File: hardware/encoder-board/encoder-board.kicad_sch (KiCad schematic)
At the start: 26 parts, among them J1 Conn_01x04, U1 ITR1204SR10A_TR(BY), U2 ITR1204SR10A_TR(BY), U3 LM2903

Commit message: various experiments with firmware. Nothing is working yet
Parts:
- R5: value 30 -> 130
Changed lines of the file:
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@@
 		(fields_autoplaced yes)
 		(property "Reference" "R5"
-			(at 207.01 54.61 0)
+			(at 207.01 54.6099 0)
 			(effects
 				(font
@@
 			)
 		)
-		(property "Value" "30"
-			(at 207.01 57.15 0)
+		(property "Value" "130"
+			(at 207.01 57.1499 0)
 			(effects
 				(font

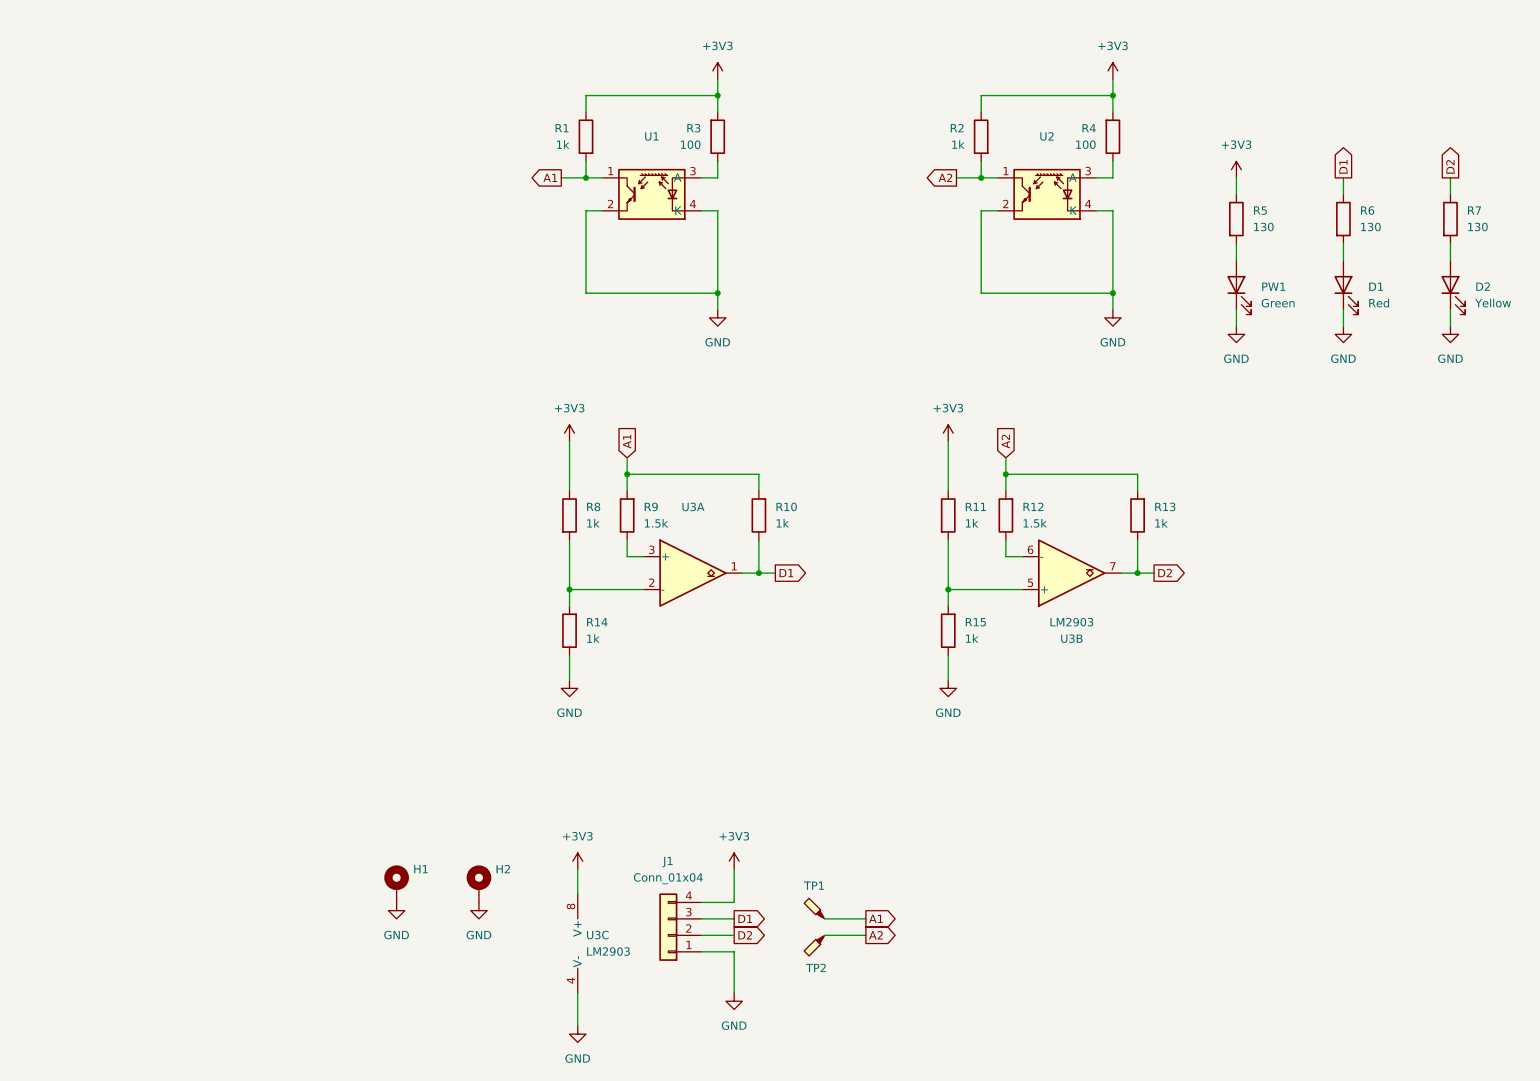
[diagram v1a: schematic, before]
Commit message: simplify encoder board to output analog output
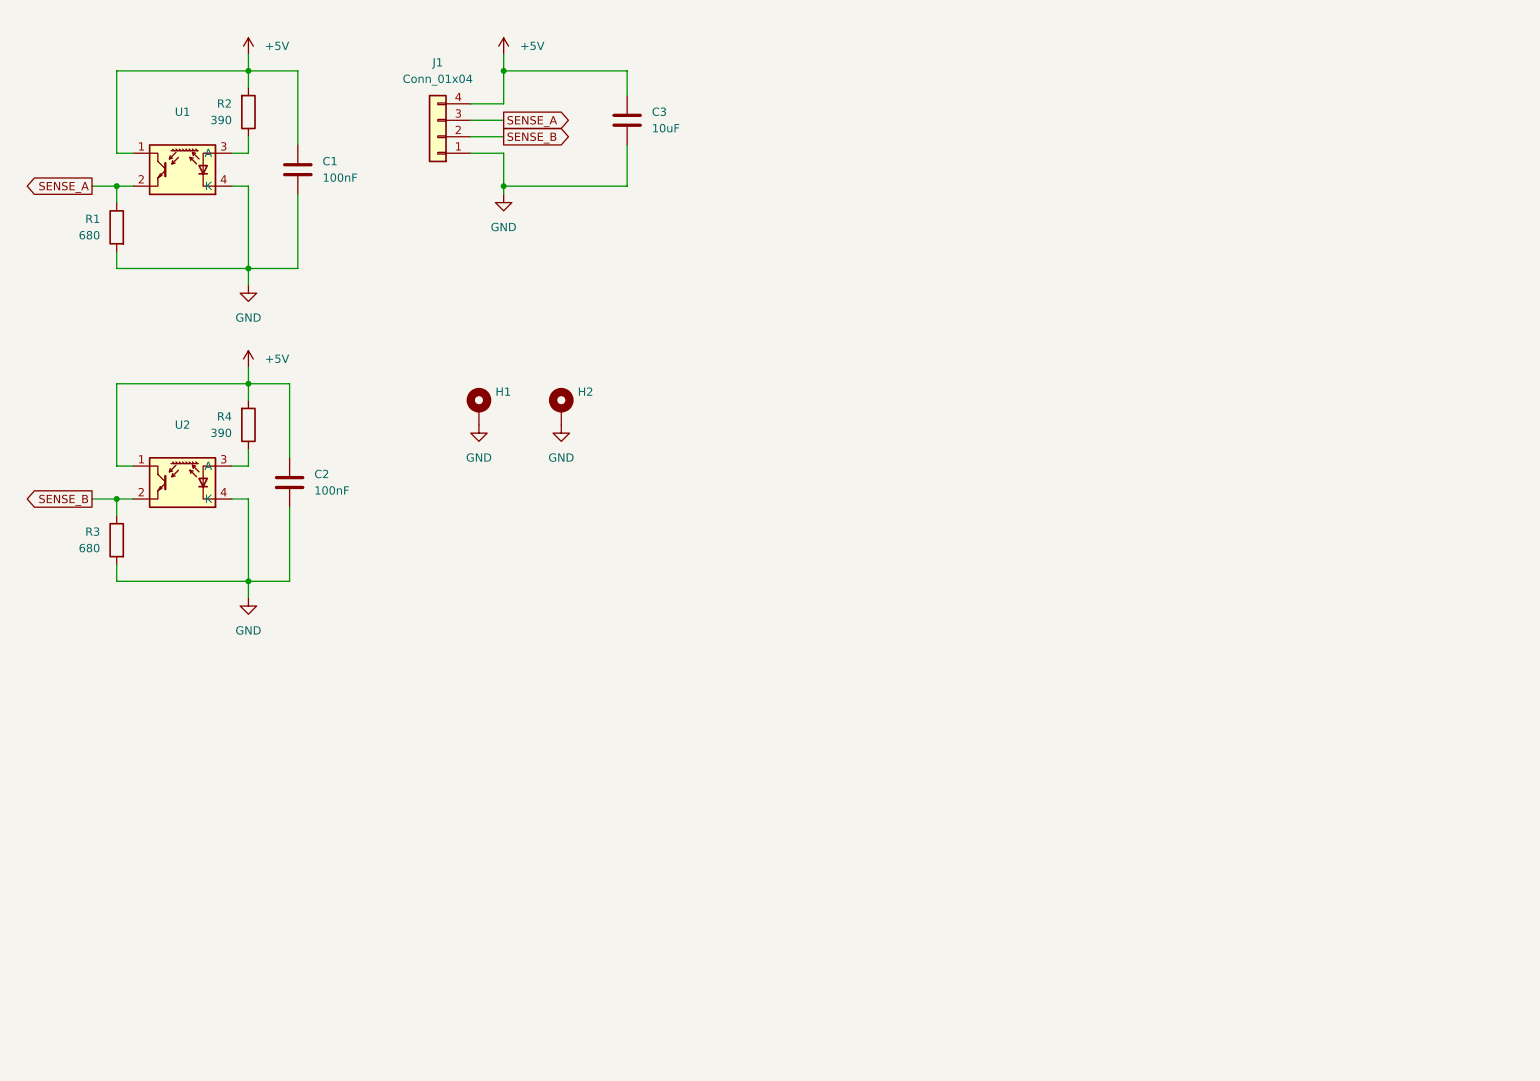
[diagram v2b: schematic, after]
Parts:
- removed D1: Red, LED_SMD:LED_0603_1608Metric, symbol Device:LED
- removed D2: Yellow, LED_SMD:LED_0603_1608Metric, symbol Device:LED
- removed PW1: Green, LED_SMD:LED_0603_1608Metric, symbol Device:LED
- removed R10, R11, R13, R14, R15, R8: 1k, Resistor_SMD:R_0603_1608Metric, symbol Device:R
- removed R12, R9: 1.5k, Resistor_SMD:R_0603_1608Metric, symbol Device:R
- removed R5, R6, R7: 130, Resistor_SMD:R_0603_1608Metric, symbol Device:R
- removed TP1, TP2: ~, TestPoint:TestPoint_Pad_D1.0mm, symbol Connector:TestPoint_Probe
- removed U3: LM2903, Package_SO:SOIC-8_3.9x4.9mm_P1.27mm, symbol Comparator:LM2903
- added C1, C2: 100nF, symbol Device:C
- added C3: 10uF, symbol Device:C
- R1: value 1k -> 680
- R2: renamed from R3; value 100 -> 390
- R3: renamed from R2; value 1k -> 680
- R4: value 100 -> 390
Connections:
- net GND: now also R1.2, R3.2, C1.2, C2.2, C3.2; no longer U1.2, U2.2
- net +3V3 renamed +5V
- net +5V: now also U1.1, U2.1, C1.1, C2.1, C3.1; no longer R1.1, R3.1
- removed net A1: R1.2, U1.1
- removed net A2: R3.2, U2.1
- net D1 renamed SENSE_A
- net SENSE_A: now also R1.1, U1.2
- net D2 renamed SENSE_B
- net SENSE_B: now also R3.1, U2.2
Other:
- moved on the sheet: H1, H2, J1, R1, R2, R3, R4, U1, U2

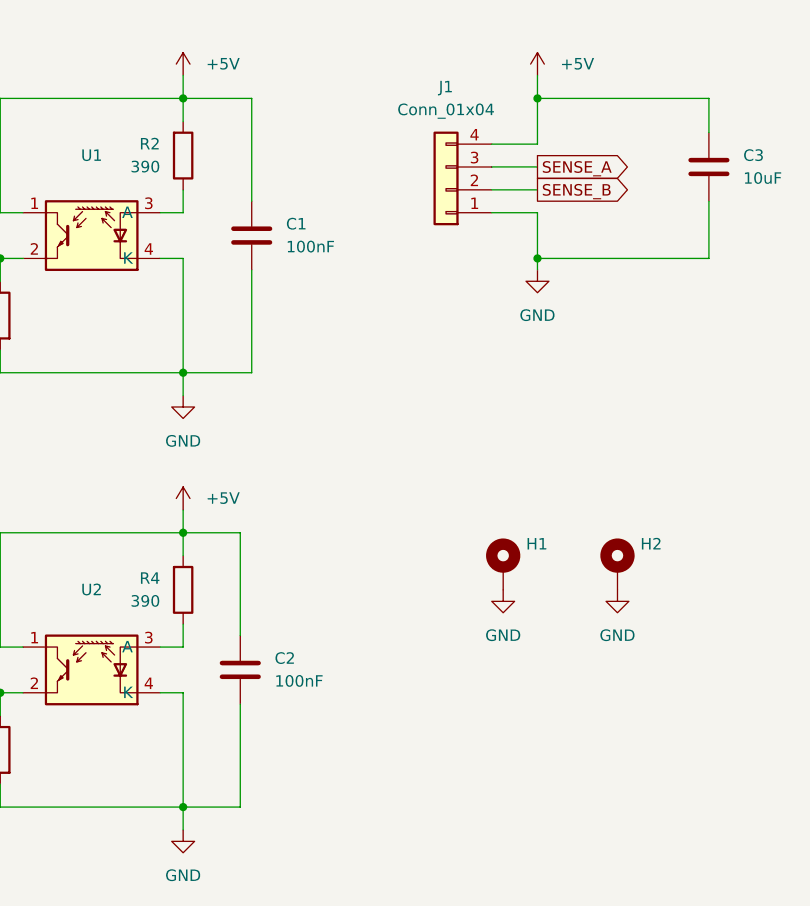
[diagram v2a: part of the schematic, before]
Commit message: remake encoder board pcb. generated jlcpcb production files.
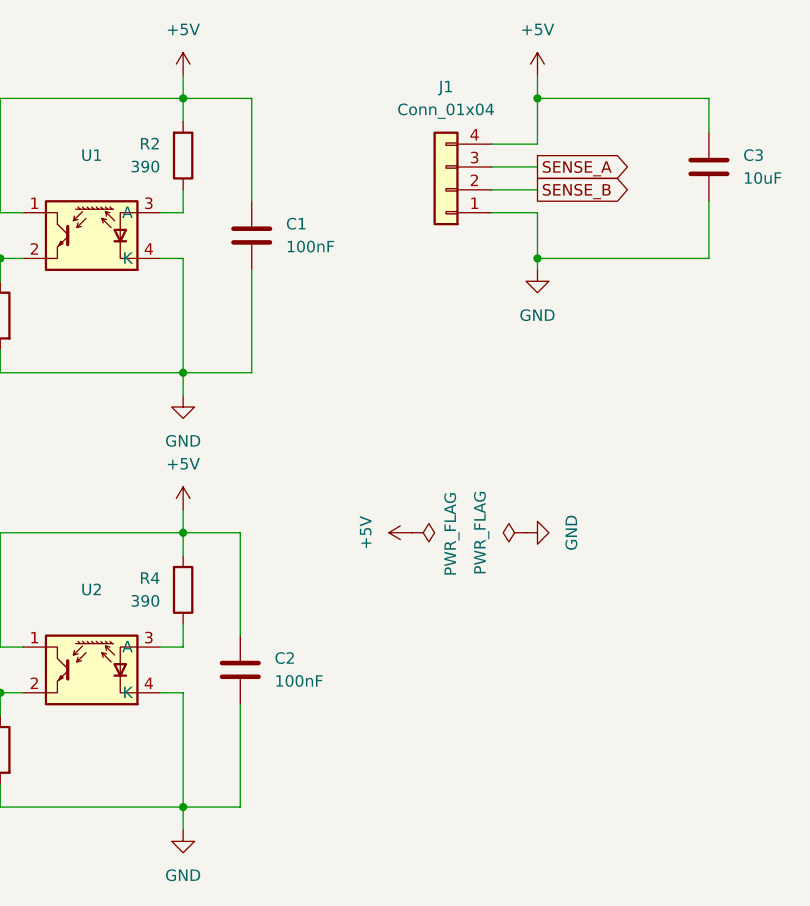
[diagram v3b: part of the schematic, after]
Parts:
- removed H1, H2: MountingHole_Pad, MountingHole:MountingHole_2.2mm_M2_ISO7380_Pad, symbol Mechanical:MountingHole_Pad
- C1, C2, C3: footprint (none) -> Capacitor_SMD:C_0805_2012Metric_Pad1.18x1.45mm_HandSolder
- J1: footprint Connector_PinHeader_2.54mm:PinHeader_1x04_P2.54mm_Vertical_SMD_Pin1Right -> Connector_PinHeader_2.54mm:PinHeader_1x04_P2.54mm_Vertical
- R1, R2, R3, R4: footprint Resistor_SMD:R_0603_1608Metric -> Resistor_SMD:R_0805_2012Metric_Pad1.20x1.40mm_HandSolder
